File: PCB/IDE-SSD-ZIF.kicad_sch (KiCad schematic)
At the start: 84 parts, among them J1 Conn_01x40_Female, U1 SM2236, U2 LP38691SD-1.8, U3 FlashBGA152, U4 FlashBGA152, U5 FlashBGA152, U6 FlashBGA152

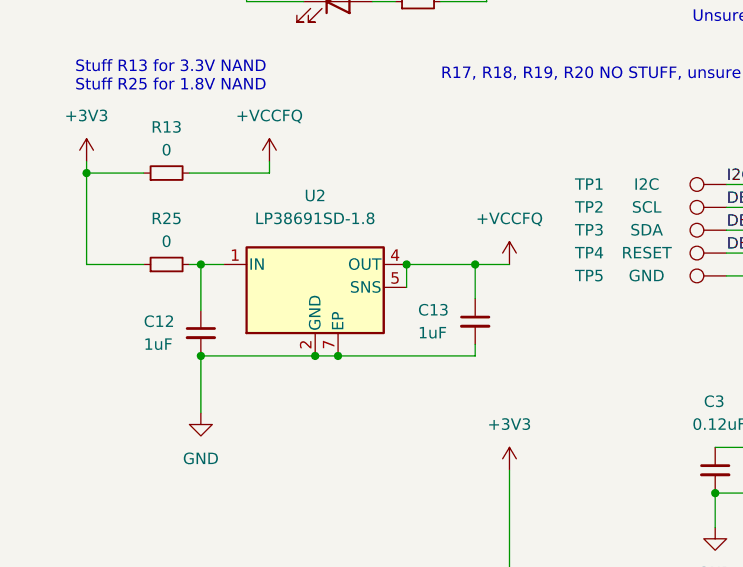
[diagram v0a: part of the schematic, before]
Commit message: Changed 1.8V reg
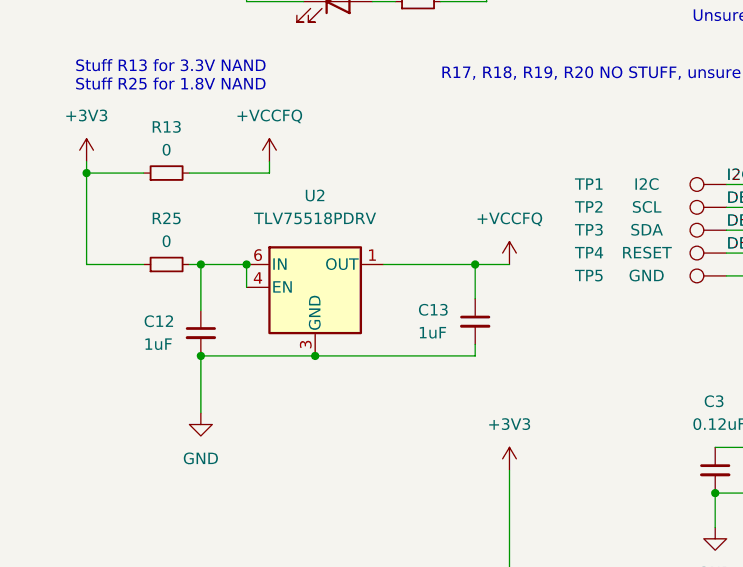
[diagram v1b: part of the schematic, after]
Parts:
- removed U2: LP38691SD-1.8, Package_SON:WSON-6-1EP_3x3mm_P0.95mm, symbol Regulator_Linear:LP38691SD-1.8
- added U2: TLV75518PDRV, Package_SON:WSON-6-1EP_2x2mm_P0.65mm_EP1x1.6mm, symbol Regulator_Linear:TLV75518PDRV
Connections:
- net +VCCFQ: now also U2.1 (OUT)
- net GND: now also U2.3 (GND), U2.7 (GND)
- net at C12.1, R25.2: now also U2.4 (EN), U2.6 (IN)
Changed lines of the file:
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@@
   (junction (at 270.51 168.91) (diameter 0) (color 0 0 0 0)
   )
-  (junction (at 46.99 186.69) (diameter 0) (color 0 0 0 0)
-  )
   (junction (at 361.95 39.37) (diameter 0) (color 0 0 0 0)
   )
@@
   (junction (at 168.91 228.6) (diameter 0) (color 0 0 0 0)
   )
-  (junction (at 57.15 176.53) (diameter 0) (color 0 0 0 0)
-  )
   (junction (at 210.82 46.99) (diameter 0) (color 0 0 0 0)
   )
@@
   (junction (at 91.44 201.93) (diameter 0) (color 0 0 0 0)
   )
+  (junction (at 46.99 186.69) (diameter 0) (color 0 0 0 0)
+  )
   (junction (at 129.54 220.98) (diameter 0) (color 0 0 0 0)
   )
@@
   (junction (at 129.54 240.03) (diameter 0) (color 0 0 0 0)
   )
+  (junction (at 39.37 176.53) (diameter 0) (color 0 0 0 0)
+  )
   (junction (at 361.95 26.67) (diameter 0) (color 0 0 0 0)
   )
@@
   (junction (at 201.93 92.71) (diameter 0) (color 0 0 0 0)
   )
-  (junction (at 49.53 186.69) (diameter 0) (color 0 0 0 0)
-  )
   (junction (at 351.79 179.07) (diameter 0) (color 0 0 0 0)
   )
@@
     (stroke (width 0) (type default) (color 0 0 0 0))
   )
-  (wire (pts (xy 46.99 186.69) (xy 49.53 186.69))
-    (stroke (width 0) (type default) (color 0 0 0 0))
-  )
   (wire (pts (xy 212.09 168.91) (xy 199.39 168.91))
     (stroke (width 0) (type default) (color 0 0 0 0))
@@
     (stroke (width 0) (type default) (color 0 0 0 0))
   )
-  (wire (pts (xy 64.77 186.69) (xy 49.53 186.69))
-    (stroke (width 0) (type default) (color 0 0 0 0))
-  )
   (bus (pts (xy 114.3 36.83) (xy 114.3 34.29))
     (stroke (width 0) (type default) (color 0 0 0 0))
@@
     (stroke (width 0) (type default) (color 0 0 0 0))
   )
-  (wire (pts (xy 34.29 186.69) (xy 46.99 186.69))
-    (stroke (width 0) (type default) (color 0 0 0 0))
-  )
   (wire (pts (xy 76.2 48.26) (xy 95.25 48.26))
     (stroke (width 0) (type default) (color 0 0 0 0))
@@
     (stroke (width 0) (type default) (color 0 0 0 0))
   )
-  (wire (pts (xy 34.29 176.53) (xy 36.83 176.53))
+  (wire (pts (xy 34.29 176.53) (xy 39.37 176.53))
     (stroke (width 0) (type default) (color 0 0 0 0))
   )
@@
     (stroke (width 0) (type default) (color 0 0 0 0))
   )
+  (wire (pts (xy 54.61 176.53) (xy 64.77 176.53))
+    (stroke (width 0) (type default) (color 0 0 0 0))
+  )
   (wire (pts (xy 116.84 82.55) (xy 129.54 82.55))
     (stroke (width 0) (type default) (color 0 0 0 0))
@@
     (stroke (width 0) (type default) (color 0 0 0 0))
   )
+  (wire (pts (xy 34.29 186.69) (xy 46.99 186.69))
+    (stroke (width 0) (type default) (color 0 0 0 0))
+  )
   (bus (pts (xy 316.23 52.07) (xy 316.23 54.61))
     (stroke (width 0) (type default) (color 0 0 0 0))
@@
     (stroke (width 0) (type default) (color 0 0 0 0))
   )
+  (wire (pts (xy 46.99 186.69) (xy 64.77 186.69))
+    (stroke (width 0) (type default) (color 0 0 0 0))
+  )
   (wire (pts (xy 16.51 22.86) (xy 24.13 22.86))
     (stroke (width 0) (type default) (color 0 0 0 0))
@@
     (stroke (width 0) (type default) (color 0 0 0 0))
   )
-  (wire (pts (xy 57.15 176.53) (xy 64.77 176.53))
-    (stroke (width 0) (type default) (color 0 0 0 0))
-  )
   (bus (pts (xy 114.3 77.47) (xy 114.3 74.93))
     (stroke (width 0) (type default) (color 0 0 0 0))
@@
     (stroke (width 0) (type default) (color 0 0 0 0))
   )
+  (wire (pts (xy 39.37 176.53) (xy 39.37 179.07))
+    (stroke (width 0) (type default) (color 0 0 0 0))
+  )
   (wire (pts (xy 283.21 38.1) (xy 283.21 39.37))
     (stroke (width 0) (type default) (color 0 0 0 0))
@@
     (stroke (width 0) (type default) (color 0 0 0 0))
   )
-  (wire (pts (xy 57.15 176.53) (xy 57.15 179.07))
-    (stroke (width 0) (type default) (color 0 0 0 0))
-  )
   (bus (pts (xy 195.58 64.77) (xy 195.58 67.31))
     (stroke (width 0) (type default) (color 0 0 0 0))
@@
     (pin "2")
   )
+  (symbol (lib_id "Regulator_Linear:TLV75518PDRV") (at 46.99 179.07 0) (unit 1)
+    (in_bom yes) (on_board yes) (fields_autoplaced)
+    (property "Reference" "U2" (id 0) (at 46.99 168.91 0))
+    (property "Value" "TLV75518PDRV" (id 1) (at 46.99 171.45 0))
+    (property "Footprint" "Package_SON:WSON-6-1EP_2x2mm_P0.65mm_EP1x1.6mm" (id 2) (at 46.99 170.815 0)
+      (effects (font (size 1.27 1.27) italic) hide)
+    )
+    (property "Datasheet" "http://www.ti.com/lit/ds/symlink/tlv755p.pdf" (id 3) (at 46.99 177.8 0)
+      (effects (font (size 1.27 1.27)) hide)
+    )
+    (pin "1")
+    (pin "2")
+    (pin "3")
+    (pin "4")
+    (pin "5")
+    (pin "6")
+    (pin "7")
+  )
   (symbol (lib_id "power:GND") (at 91.44 205.74 0) (unit 1)
     (in_bom yes) (on_board yes) (fields_autoplaced)
@@
     (pin "1")
   )
-  (symbol (lib_id "Regulator_Linear:LP38691SD-1.8") (at 46.99 179.07 0) (unit 1)
-    (in_bom yes) (on_board yes) (fields_autoplaced)
-    (property "Reference" "U2" (id 0) (at 46.99 168.91 0))
-    (property "Value" "LP38691SD-1.8" (id 1) (at 46.99 171.45 0))
-    (property "Footprint" "Package_SON:WSON-6-1EP_3x3mm_P0.95mm" (id 2) (at 46.99 179.07 0)
-      (effects (font (size 1.27 1.27)) hide)
-    )
-    (property "Datasheet" "https://www.ti.com/lit/ds/symlink/lp38691.pdf" (id 3) (at 46.99 179.07 0)
-      (effects (font (size 1.27 1.27)) hide)
-    )
-    (pin "1")
-    (pin "2")
-    (pin "3")
-    (pin "4")
-    (pin "5")
-    (pin "6")
-    (pin "7")
-  )
   (symbol (lib_id "Connector:TestPoint") (at 92.71 172.72 90) (unit 1)
     (in_bom yes) (on_board yes)
@@
       (reference "U1") (unit 1) (value "SM2236") (footprint "cust:BGA-144_12x12_9.0x9.0mm")
     )
-    (path "/ebe9401d-3e91-46ac-a2b2-7ef86752e4e0"
-      (reference "U2") (unit 1) (value "LP38691SD-1.8") (footprint "Package_SON:WSON-6-1EP_3x3mm_P0.95mm")
+    (path "/aecb8b29-acf8-488c-bc22-13c0893bad2d"
+      (reference "U2") (unit 1) (value "TLV75518PDRV") (footprint "Package_SON:WSON-6-1EP_2x2mm_P0.65mm_EP1x1.6mm")
     )
     (path "/ceba4065-2a56-47ca-a8fb-2a3e07d4063c"

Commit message: Fixed regulator footprint
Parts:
- U2: footprint Package_SON:WSON-6-1EP_2x2mm_P0.65mm_EP1x1.6mm -> cust:WSON-6-1EP_2x2mm_P0.65mm_EP1x1.6mm
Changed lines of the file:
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@@
     (property "Reference" "U2" (id 0) (at 46.99 168.91 0))
     (property "Value" "TLV75518PDRV" (id 1) (at 46.99 171.45 0))
-    (property "Footprint" "Package_SON:WSON-6-1EP_2x2mm_P0.65mm_EP1x1.6mm" (id 2) (at 46.99 170.815 0)
+    (property "Footprint" "cust:WSON-6-1EP_2x2mm_P0.65mm_EP1x1.6mm" (id 2) (at 46.99 170.815 0)
       (effects (font (size 1.27 1.27) italic) hide)
     )
@@
     )
     (path "/aecb8b29-acf8-488c-bc22-13c0893bad2d"
-      (reference "U2") (unit 1) (value "TLV75518PDRV") (footprint "Package_SON:WSON-6-1EP_2x2mm_P0.65mm_EP1x1.6mm")
+      (reference "U2") (unit 1) (value "TLV75518PDRV") (footprint "cust:WSON-6-1EP_2x2mm_P0.65mm_EP1x1.6mm")
     )
     (path "/ceba4065-2a56-47ca-a8fb-2a3e07d4063c"
